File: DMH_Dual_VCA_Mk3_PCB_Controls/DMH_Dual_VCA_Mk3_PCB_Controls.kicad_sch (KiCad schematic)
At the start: 58 parts, among them J1 TRS_Jack_6.35mm_Sw, J10 IDC_02x05, J11 Conn_01x06, J12 Conn_01x08, J13 Conn_01x06, J14 Conn_01x06, J15 Conn_01x08, J16 Conn_01x06, J17 IDC_02x05, J18 Conn_02x03_Odd_Even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

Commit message: Controls PCB comp placement started
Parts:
- J12: footprint Connector_PinSocket_2.54mm:PinSocket_1x06_P2.54mm_Vertical -> Connector_PinSocket_2.54mm:PinSocket_1x08_P2.54mm_Vertical
- J15: footprint Connector_PinHeader_2.54mm:PinHeader_1x06_P2.54mm_Vertical -> Connector_PinHeader_2.54mm:PinHeader_1x08_P2.54mm_Vertical
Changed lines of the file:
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@@
 			)
 		)
-		(property "Footprint" "Connector_PinSocket_2.54mm:PinSocket_1x06_P2.54mm_Vertical"
+		(property "Footprint" "Connector_PinSocket_2.54mm:PinSocket_1x08_P2.54mm_Vertical"
 			(at 101.6 195.58 0)
 			(hide yes)
@@
 			(at 101.6 195.58 0)
 			(hide yes)
+			(show_name no)
+			(do_not_autoplace no)
+			(effects
+				(font
+					(size 1.27 1.27)
+				)
+			)
+		)
+		(property "Function" ""
+			(at 101.6 195.58 0)
 			(show_name no)
 			(do_not_autoplace no)
@@
 			)
 		)
-		(property "Footprint" "Connector_PinHeader_2.54mm:PinHeader_1x06_P2.54mm_Vertical"
+		(property "Footprint" "Connector_PinHeader_2.54mm:PinHeader_1x08_P2.54mm_Vertical"
 			(at 139.7 195.58 0)
 			(hide yes)
@@
 			(show_name no)
 			(do_not_autoplace no)
+			(effects
+				(font
+					(size 1.27 1.27)
+				)
+			)
+		)
+		(property "Function" ""
+			(at 139.7 195.58 0)
+			(show_name no)
+			(do_not_autoplace no)

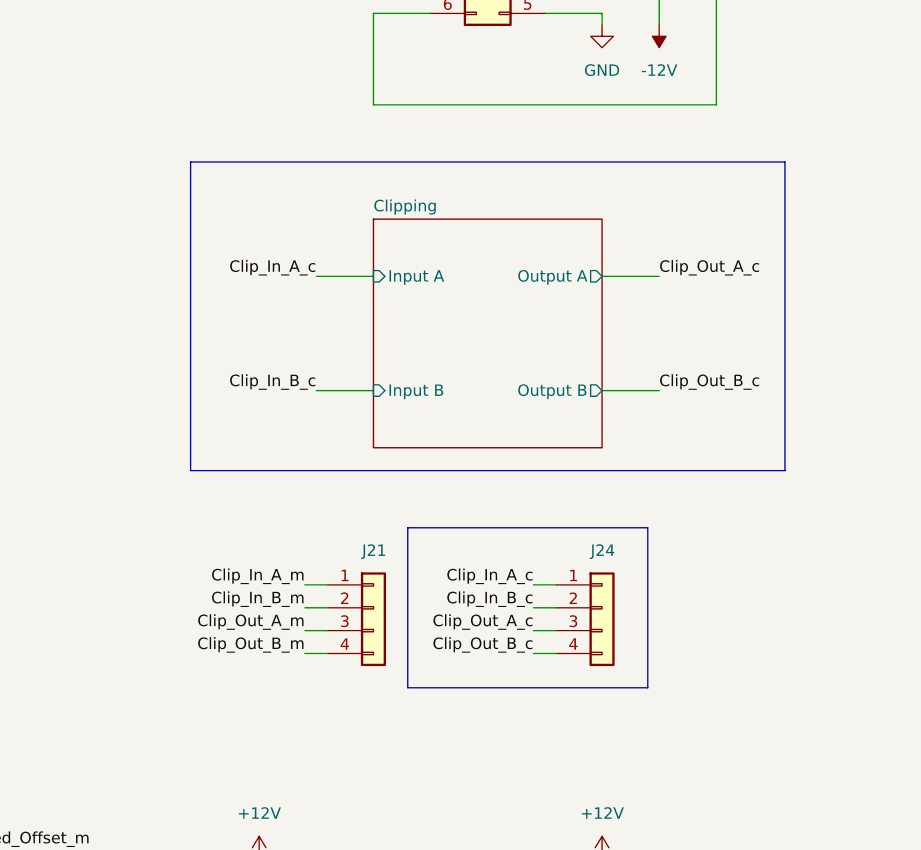
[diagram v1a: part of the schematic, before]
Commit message: Moved clipping circuit back to main PCB
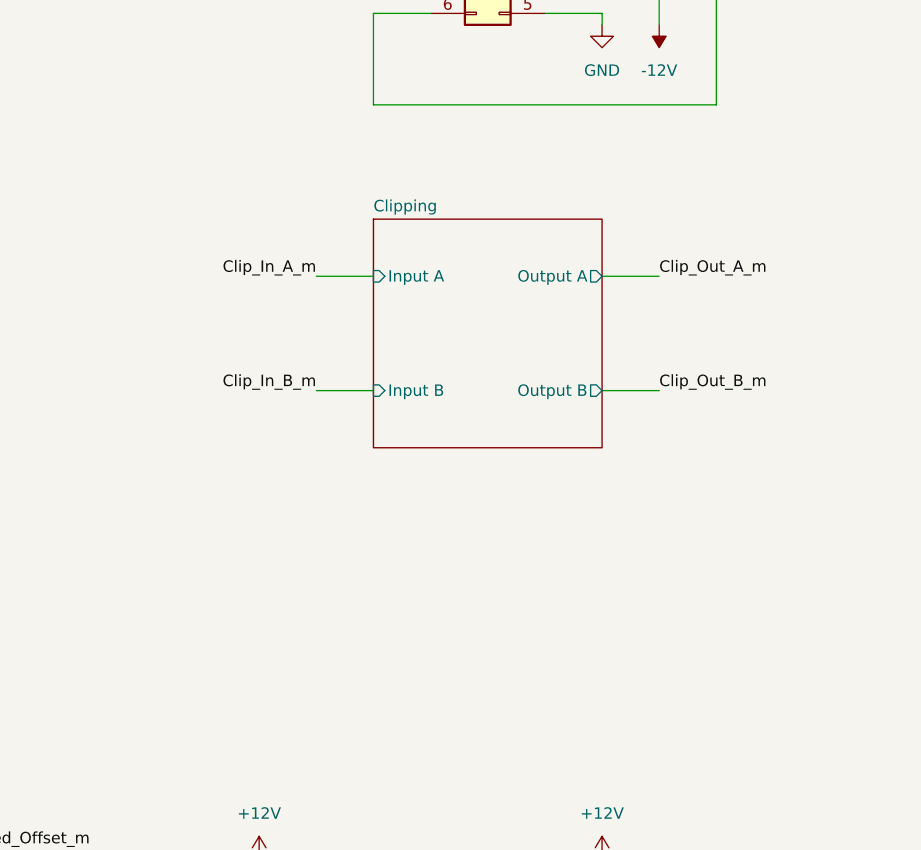
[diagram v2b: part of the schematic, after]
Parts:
- removed J21: Conn_01x04, Connector_PinHeader_2.54mm:PinHeader_1x04_P2.54mm_Vertical, symbol Connector_Generic:Conn_01x04
- removed J24: Conn_01x04, Connector_PinSocket_2.54mm:PinSocket_1x04_P2.54mm_Vertical, symbol Connector_Generic:Conn_01x04

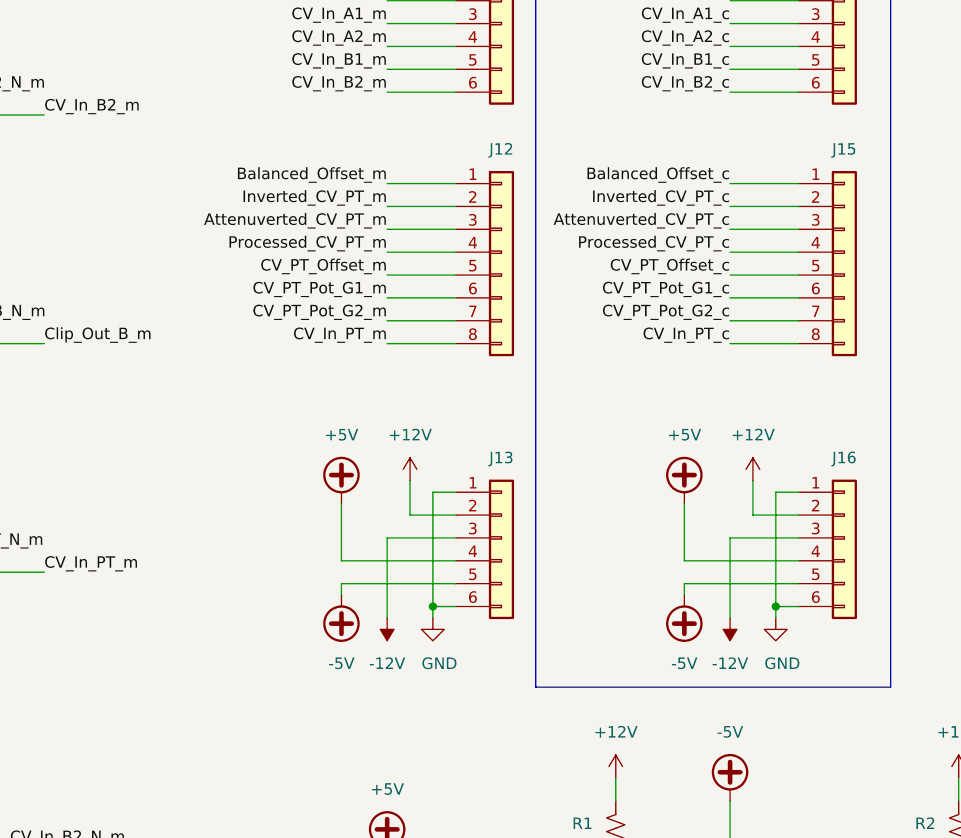
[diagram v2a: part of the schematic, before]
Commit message: Controls PCB comp placement in progress
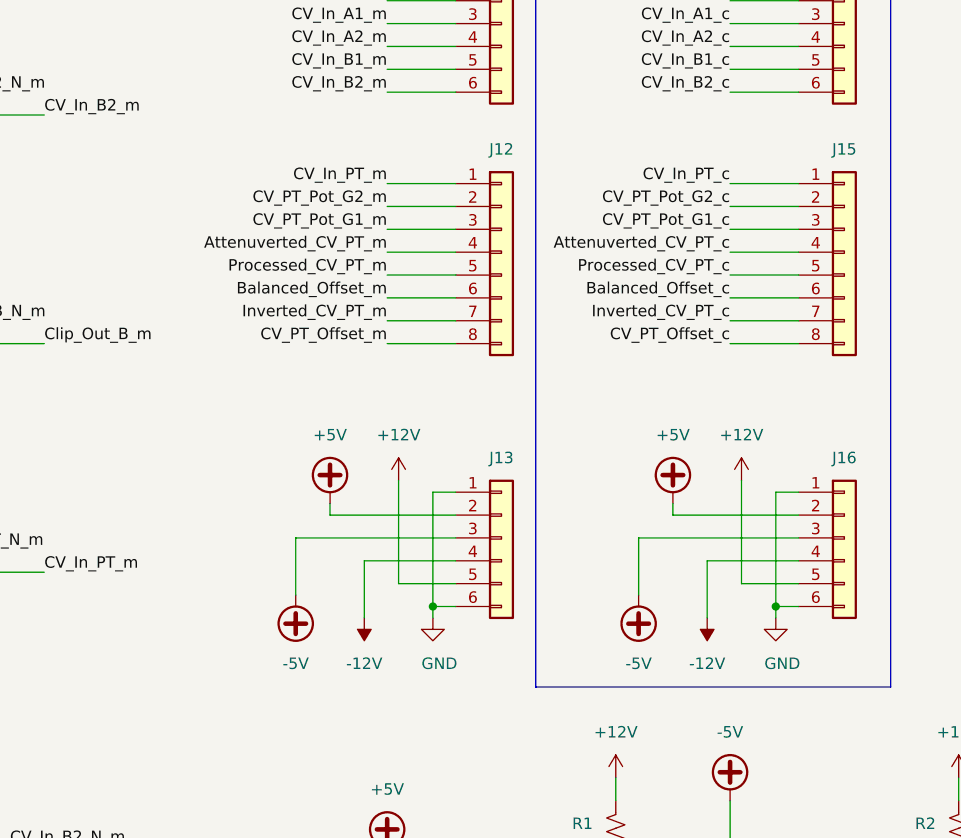
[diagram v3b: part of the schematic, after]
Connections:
- net +12V: now also J13.5 (Pin_5), J16.5 (Pin_5); no longer J13.2 (Pin_2), J16.2 (Pin_2)
- net +5V: now also J13.2 (Pin_2), J16.2 (Pin_2); no longer J13.4 (Pin_4), J16.4 (Pin_4)
- net -12V: now also J13.4 (Pin_4), J16.4 (Pin_4); no longer J13.3 (Pin_3), J16.3 (Pin_3)
- net -5V: now also J13.3 (Pin_3), J16.3 (Pin_3); no longer J13.5 (Pin_5), J16.5 (Pin_5)
- net Attenuverted_CV_PT_c: now also J15.4 (Pin_4); no longer J15.3 (Pin_3)
- net Attenuverted_CV_PT_m: now also J12.4 (Pin_4); no longer J12.3 (Pin_3)
- net Balanced_Offset_c: now also J15.6 (Pin_6); no longer J15.1 (Pin_1)
- net Balanced_Offset_m: now also J12.6 (Pin_6); no longer J12.1 (Pin_1)
- net CV_In_PT_c: now also J15.1 (Pin_1); no longer J15.8 (Pin_8)
- net CV_In_PT_m: now also J12.1 (Pin_1); no longer J12.8 (Pin_8)
- net CV_PT_Offset_c: now also J15.8 (Pin_8); no longer J15.5 (Pin_5)
- net CV_PT_Offset_m: now also J12.8 (Pin_8); no longer J12.5 (Pin_5)
- net CV_PT_Pot_G1_c: now also J15.3 (Pin_3); no longer J15.6 (Pin_6)
- net CV_PT_Pot_G1_m: now also J12.3 (Pin_3); no longer J12.6 (Pin_6)
- net CV_PT_Pot_G2_c: now also J15.2 (Pin_2); no longer J15.7 (Pin_7)
- net CV_PT_Pot_G2_m: now also J12.2 (Pin_2); no longer J12.7 (Pin_7)
- net Inverted_CV_PT_c: now also J15.7 (Pin_7); no longer J15.2 (Pin_2)
- net Inverted_CV_PT_m: now also J12.7 (Pin_7); no longer J12.2 (Pin_2)
- net Processed_CV_PT_c: now also J15.5 (Pin_5); no longer J15.4 (Pin_4)
- net Processed_CV_PT_m: now also J12.5 (Pin_5); no longer J12.4 (Pin_4)

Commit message: Controls PCB comp placement done
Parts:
- J14, J16: footprint Connector_PinHeader_2.54mm:PinHeader_1x06_P2.54mm_Vertical -> Connector_PinSocket_2.54mm:PinSocket_1x06_P2.54mm_Vertical
- J15: footprint Connector_PinHeader_2.54mm:PinHeader_1x08_P2.54mm_Vertical -> Connector_PinSocket_2.54mm:PinSocket_1x08_P2.54mm_Vertical
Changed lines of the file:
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@@
 			)
 		)
-		(property "Footprint" "Connector_PinHeader_2.54mm:PinHeader_1x08_P2.54mm_Vertical"
+		(property "Footprint" "Connector_PinSocket_2.54mm:PinSocket_1x08_P2.54mm_Vertical"
 			(at 139.7 195.58 0)
 			(hide yes)
@@
 			)
 		)
-		(property "Footprint" "Connector_PinHeader_2.54mm:PinHeader_1x06_P2.54mm_Vertical"
+		(property "Footprint" "Connector_PinSocket_2.54mm:PinSocket_1x06_P2.54mm_Vertical"
 			(at 139.7 170.18 0)
 			(hide yes)
@@
 			)
 		)
-		(property "Footprint" "Connector_PinHeader_2.54mm:PinHeader_1x06_P2.54mm_Vertical"
+		(property "Footprint" "Connector_PinSocket_2.54mm:PinSocket_1x06_P2.54mm_Vertical"
 			(at 139.7 227.33 0)
 			(hide yes)

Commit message: Started Main PCB comp placement
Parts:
- J11: footprint Connector_PinSocket_2.54mm:PinSocket_1x06_P2.54mm_Vertical -> Connector_PinHeader_2.54mm:PinHeader_1x06_P2.54mm_Vertical
- J12: footprint Connector_PinSocket_2.54mm:PinSocket_1x08_P2.54mm_Vertical -> Connector_PinHeader_2.54mm:PinHeader_1x08_P2.54mm_Vertical
- JP1: footprint (none) -> Connector_PinHeader_2.54mm:PinHeader_1x03_P2.54mm_Vertical
- renumbered J17 to J100, J10 to J200
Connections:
- net CV_In_A2_N_m: now also J200.6 (Pin_6); no longer J200.4 (Pin_4)
- net CV_In_B2_N_m: now also J200.8 (Pin_8); no longer J200.6 (Pin_6)
- net Input_B_N_m: now also J200.2 (Pin_2); no longer J200.9 (Pin_9)
- net Output_A_N_m: now also J200.9 (Pin_9); no longer J200.2 (Pin_2)
- net Output_B_N_m: now also J200.4 (Pin_4); no longer J200.8 (Pin_8)
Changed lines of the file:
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@@
 	)
 	(label "Output_A_N_m"
-		(at 29.21 264.16 180)
+		(at 46.99 269.24 0)
 		(effects
 			(font
 				(size 1.27 1.27)
 			)
-			(justify right bottom)
+			(justify left bottom)
 		)
 	)
@@
 	)
 	(label "Input_B_N_m"
-		(at 46.99 269.24 0)
+		(at 29.21 264.16 180)
 		(effects
 			(font
 				(size 1.27 1.27)
 			)
-			(justify left bottom)
+			(justify right bottom)
 		)
 	)
@@
 	)
 	(label "Output_B_N_m"
-		(at 46.99 266.7 0)
+		(at 29.21 269.24 180)
 		(effects
 			(font
 				(size 1.27 1.27)
 			)
-			(justify left bottom)
+			(justify right bottom)
 		)
 	)
@@
 	)
 	(label "CV_In_B2_N_m"
-		(at 46.99 261.62 0)
+		(at 46.99 266.7 0)
 		(effects
 			(font
@@
 	)
 	(label "CV_In_A2_N_m"
-		(at 29.21 269.24 180)
+		(at 46.99 261.62 0)
 		(effects
 			(font
 				(size 1.27 1.27)
 			)
-			(justify right bottom)
+			(justify left bottom)
 		)
 	)
@@
 			)
 		)
-		(property "Footprint" "Connector_PinSocket_2.54mm:PinSocket_1x08_P2.54mm_Vertical"
+		(property "Footprint" "Connector_PinHeader_2.54mm:PinHeader_1x08_P2.54mm_Vertical"
 			(at 101.6 195.58 0)
 			(hide yes)
@@
 			)
 		)
-		(property "Footprint" "Connector_PinSocket_2.54mm:PinSocket_1x06_P2.54mm_Vertical"
+		(property "Footprint" "Connector_PinHeader_2.54mm:PinHeader_1x06_P2.54mm_Vertical"
 			(at 101.6 170.18 0)
 			(hide yes)
@@
 			)
 		)
+		(property "Function" ""
+			(at 101.6 170.18 0)
+			(show_name no)
+			(do_not_autoplace no)
+			(effects
+				(font
+					(size 1.27 1.27)
+				)
+			)
+		)
 		(pin "5"
 		)
@@
 			)
 		)
-		(property "Footprint" ""
+		(property "Footprint" "Connector_PinHeader_2.54mm:PinHeader_1x03_P2.54mm_Vertical"
 			(at 76.2 271.78 0)
 			(hide yes)
@@
 			)
 		)
+		(property "Function" ""
+			(at 76.2 271.78 0)
+			(hide yes)
+			(show_name no)
+			(do_not_autoplace no)
+			(effects
+				(font
+					(size 1.27 1.27)
+				)
+			)
+		)
 		(pin "1"
 		)
@@
 		(dnp no)
 		(fields_autoplaced yes)
-		(property "Reference" "J10"
+		(property "Reference" "J200"
 			(at 38.1 255.27 0)
 			(show_name no)
@@
 			(project "DMH_Dual_VCA_Mk3_PCB_Controls"
 				(path "/58f4306d-5387-4983-bb08-41a2313fd315"
-					(reference "J10")
+					(reference "J200")
 					(unit 1)
 				)
@@
 		(dnp no)
 		(fields_autoplaced yes)
-		(property "Reference" "J17"
+		(property "Reference" "J100"
 			(at 190.5 257.81 0)
 			(show_name no)
@@
 			(project "DMH_Dual_VCA_Mk3_PCB_Controls"
 				(path "/58f4306d-5387-4983-bb08-41a2313fd315"
-					(reference "J17")
+					(reference "J100")
 					(unit 1)
 				)

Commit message: Comp placement in progress
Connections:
- net CV_In_A1_N_m: now also J200.8 (Pin_8); no longer J200.3 (Pin_3)
- net CV_In_A2_N_m: now also J200.1 (Pin_1); no longer J200.6 (Pin_6)
- net CV_In_B2_N_m: now also J200.3 (Pin_3); no longer J200.8 (Pin_8)
- net Input_A_N_m: now also J200.6 (Pin_6); no longer J200.1 (Pin_1)
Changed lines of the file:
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@@
 	)
 	(label "Input_A_N_m"
-		(at 29.21 261.62 180)
+		(at 46.99 261.62 0)
 		(effects
 			(font
 				(size 1.27 1.27)
 			)
-			(justify right bottom)
+			(justify left bottom)
 		)
 	)
@@
 	)
 	(label "CV_In_A1_N_m"
-		(at 29.21 266.7 180)
+		(at 46.99 266.7 0)
 		(effects
 			(font
 				(size 1.27 1.27)
 			)
-			(justify right bottom)
+			(justify left bottom)
 		)
 	)
@@
 	)
 	(label "CV_In_B2_N_m"
-		(at 46.99 266.7 0)
+		(at 29.21 266.7 180)
 		(effects
 			(font
 				(size 1.27 1.27)
 			)
-			(justify left bottom)
+			(justify right bottom)
 		)
 	)
@@
 	)
 	(label "CV_In_A2_N_m"
-		(at 46.99 261.62 0)
+		(at 29.21 261.62 180)
 		(effects
 			(font
 				(size 1.27 1.27)
 			)
-			(justify left bottom)
+			(justify right bottom)
 		)
 	)

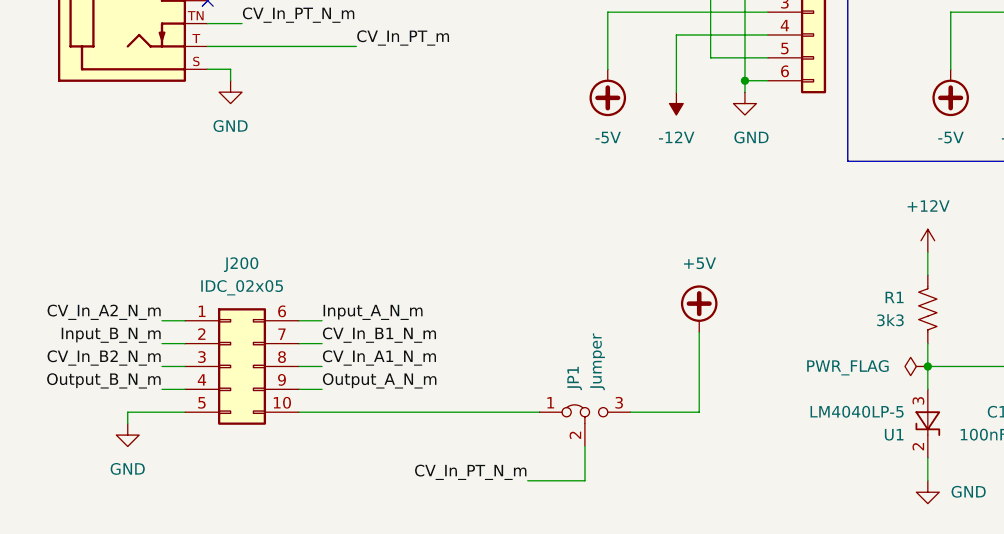
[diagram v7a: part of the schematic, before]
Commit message: Added jumpers to normalize CV inputs B to A
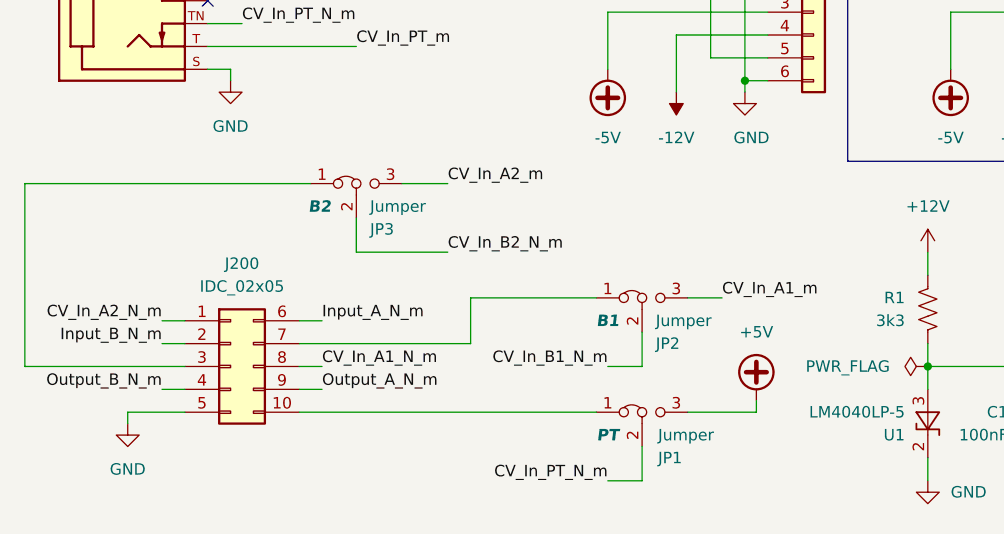
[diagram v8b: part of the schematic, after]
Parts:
- added JP2, JP3: Jumper, Connector_PinHeader_2.54mm:PinHeader_1x03_P2.54mm_Vertical, symbol Jumper:Jumper_3_Bridged12
- JP1: Function (none) -> PT; now in the parts list
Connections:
- net CV_In_A1_m: now also JP2.3 (B)
- net CV_In_A2_m: now also JP3.3 (B)
- net CV_In_B1_N_m: now also JP2.2 (C); no longer J200.7 (Pin_7)
- net CV_In_B2_N_m: now also JP3.2 (C); no longer J200.3 (Pin_3)
- new net: J200.7 (Pin_7), JP2.1 (A)
- new net: J200.3 (Pin_3), JP3.1 (A)
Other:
- moved on the sheet: JP1
